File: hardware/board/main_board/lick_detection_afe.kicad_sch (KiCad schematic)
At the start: 77 parts, among them J3 Conn_Triaxial, U10 ADA4891-2, U13 ADS7049, U14 MAX4564EKA, U15 MAX4564EKA, U6 ADA4891-4, U7 LTC6268xS8-10, U8 REF2025, U9 TS5A9411DCKR

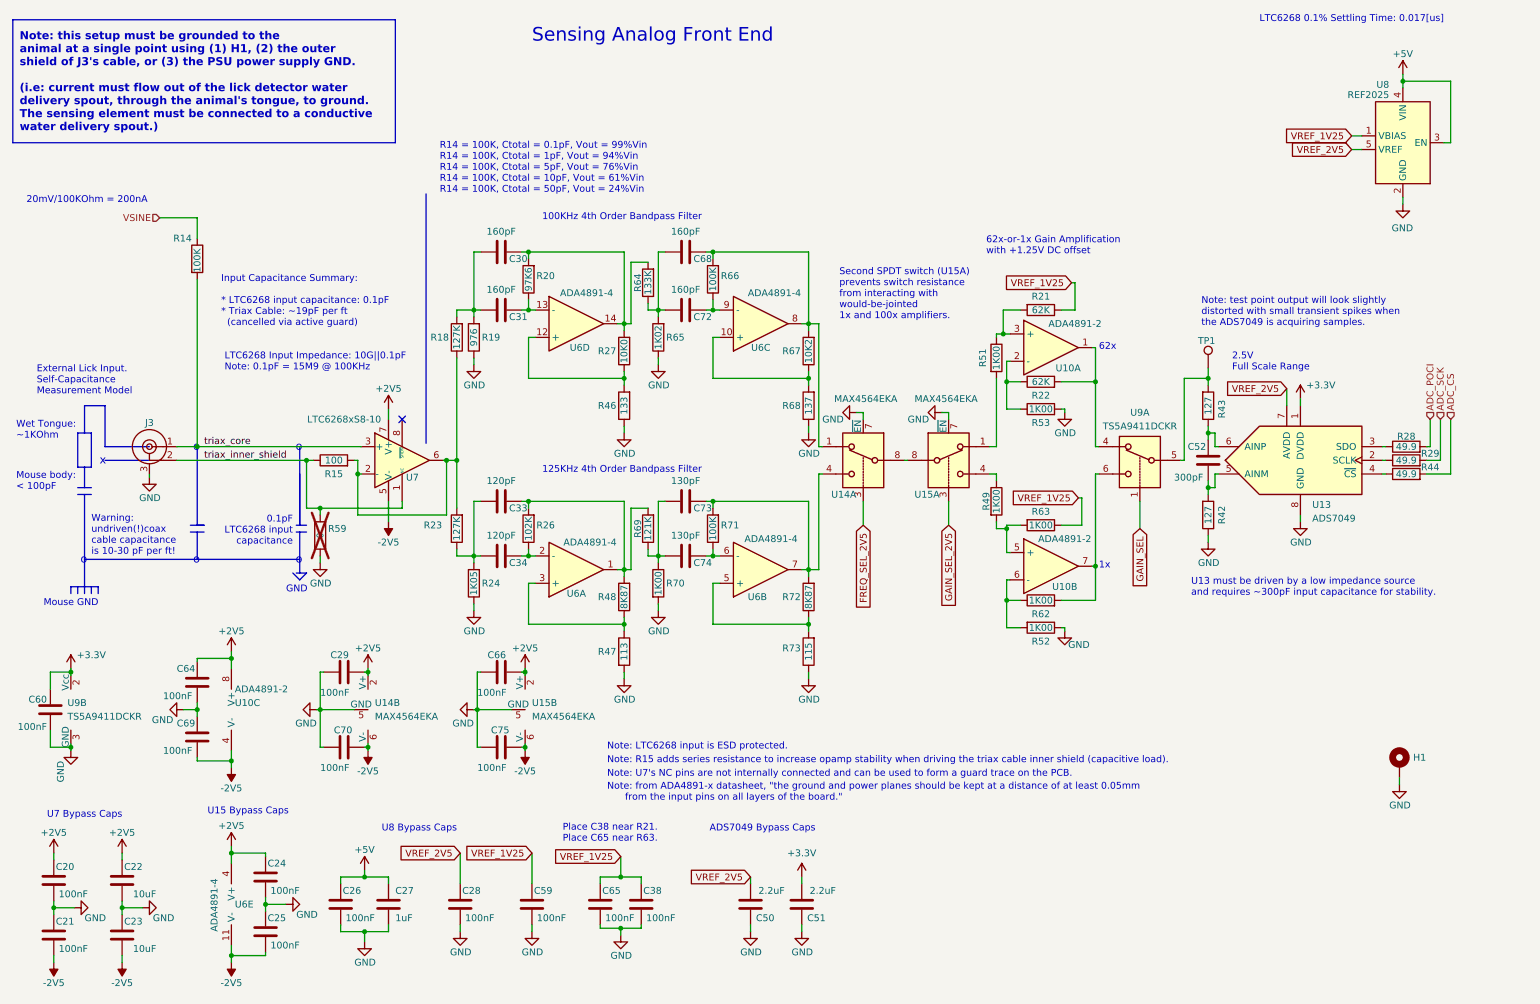
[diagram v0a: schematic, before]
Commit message: split board into two
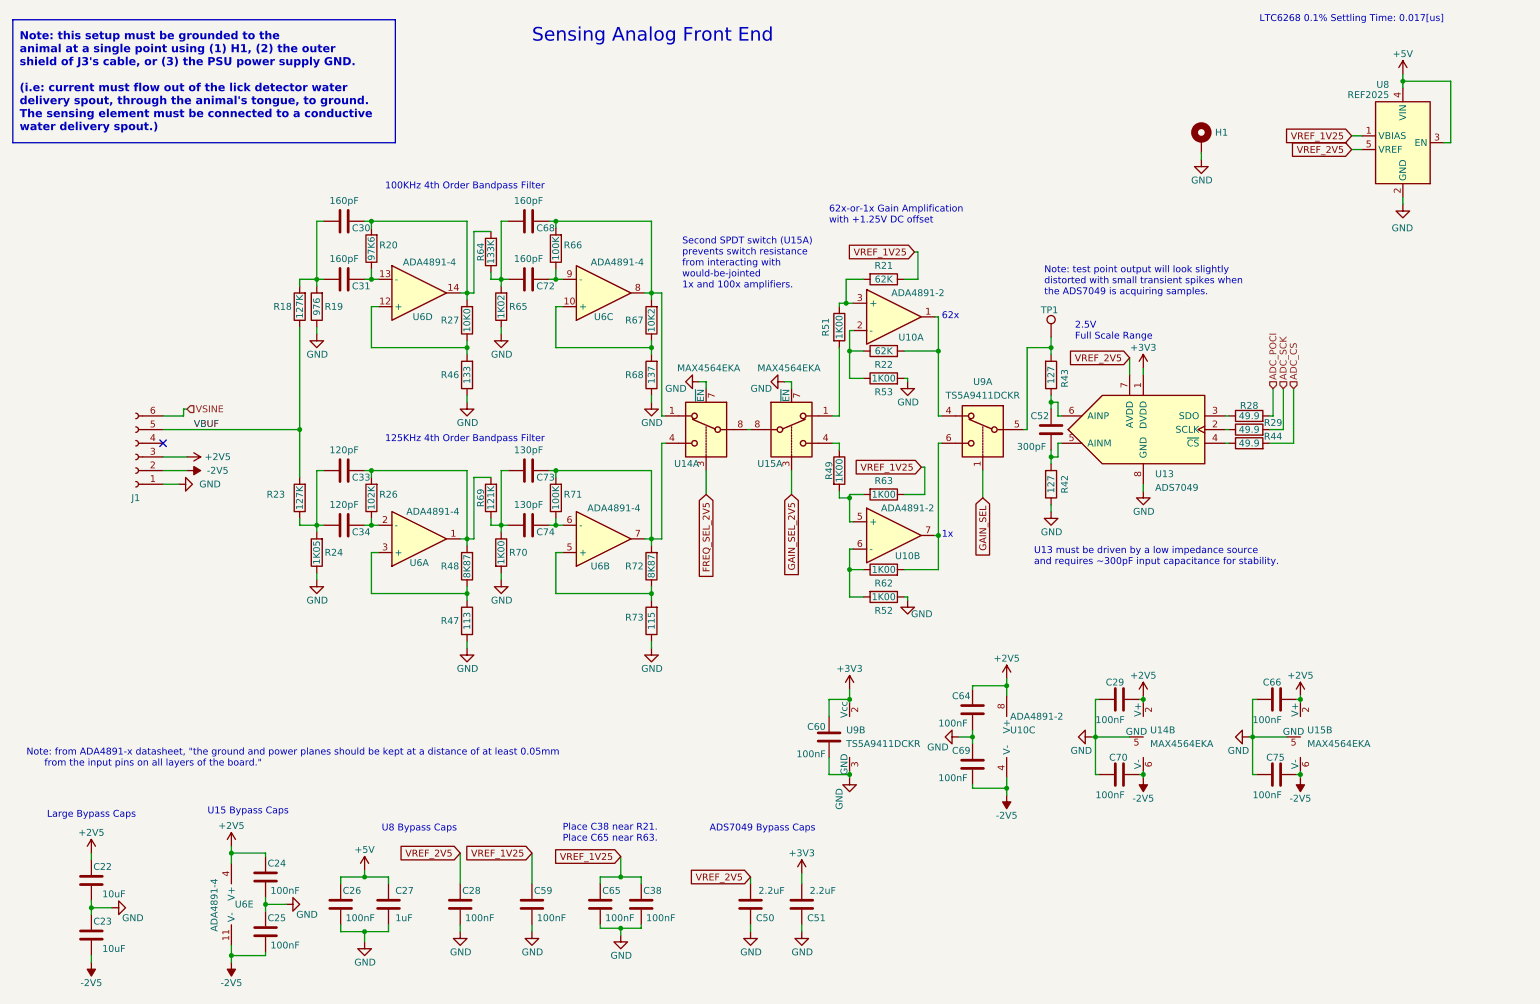
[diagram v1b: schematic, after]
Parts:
- removed C20, C21: 100nF, Capacitor_SMD:C_0402_1005Metric, symbol Device:C
- removed J3: Conn_Triaxial, kicad_component_library:TRB_Trompeter_CBBJR79A_Horizontal, symbol kicad_component_library:Conn_Triaxial
- removed R14: 100K, Resistor_SMD:R_1206_3216Metric, symbol Device:R
- removed R15: 100, Resistor_SMD:R_0402_1005Metric_Pad0.72x0.64mm_HandSolder, symbol Device:R
- removed R59: 0, Resistor_SMD:R_0402_1005Metric_Pad0.72x0.64mm_HandSolder, symbol Device:R
- removed U7: LTC6268xS8-10, Package_SO:SO-8_3.9x4.9mm_P1.27mm, symbol Amplifier_Operational:LTC6268xS8-10
- added J1: Conn_01x06_Female, Connector_JST:JST_SH_SM06B-SRSS-TB_1x06-1MP_P1.00mm_Horizontal, symbol Connector:Conn_01x06_Female
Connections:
- net +2V5: now also J1.3 (Pin_3)
- net -2V5: now also J1.2 (Pin_2)
- net GND: now also J1.1 (Pin_1)
- net VSINE: now also J1.6 (Pin_6)
- net VBUF: now reaches R18.1, R23.2
- net VBUF: now also J1.5 (Pin_5)
- net +3.3V renamed +3V3
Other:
- note added: "Large Bypass Caps"
- note removed: "0.1pF LTC6268 input capacitance"
- note removed: "20mV/100KOhm = 200nA"
- note removed: "External Lick Input. Self-Capacitance Measurement Model"
- note removed: "GND"
- note removed: "Input Capacitance Summary: * LTC6268 input capacitance: 0.1pF * Triax Cable: ~19pF per ft (cancelled via active guard)"
- note removed: "LTC6268 Input Impedance: 10G||0.1pF Note: 0.1pF = 15M9 @ 100KHz"
- note removed: "Mouse GND"
- note removed: "Mouse body: < 100pF"
- note removed: "Note: LTC6268 input is ESD protected."
- note removed: "Note: R15 adds series resistance to increase opamp stability when driving the triax cable inner shield (capacitive load)."
- note removed: "Note: U7's NC pins are not internally connected and can be used to form a guard trace on the PCB."
- note removed: "R14 = 100K, Ctotal = 0.1pF, Vout = 99%Vin R14 = 100K, Ctotal = 1pF, Vout = 94%Vin R14 = 100K, Ctotal = 5pF, Vout = 76%Vin R14 = 100K, Ctotal = 10pF, Vout = 61%Vin R14 = 100K, Ctotal = 50pF, Vout = 24%Vin"
- note removed: "U7 Bypass Caps"
- note removed: "Warning: undriven(!)coax cable capacitance is 10-30 pF per ft!"
- note removed: "Wet Tongue: ~1KOhm"
- note removed: "o"
- note removed: "x"
- moved on the sheet: C22, C23, C29, C30, C31, C33, C34, C52, C60, C64, C66, C68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

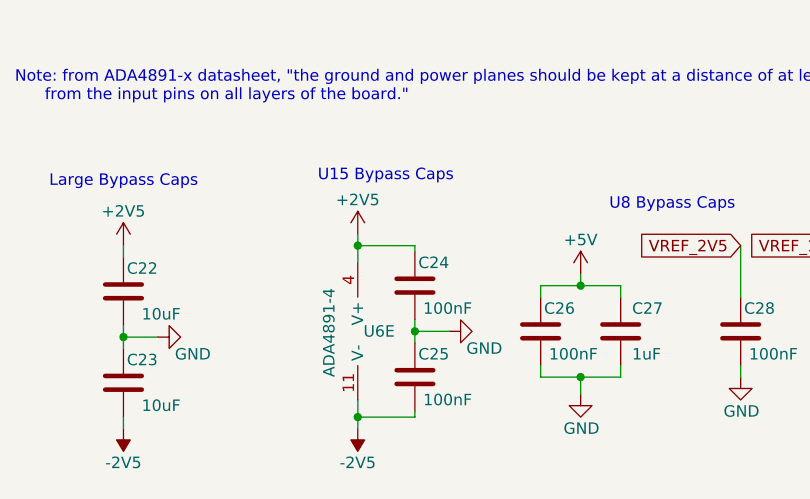
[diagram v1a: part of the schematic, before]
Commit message: update buffer board soldermask cutout
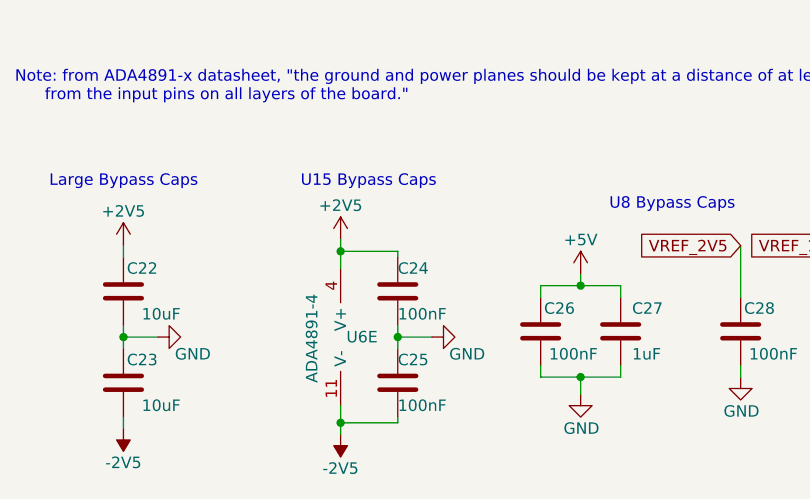
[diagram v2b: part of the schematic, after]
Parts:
- C22, C23: Alternate CL21B106KOQNNNE -> (none)
- C24, C25: footprint Capacitor_SMD:C_0603_1608Metric -> Capacitor_SMD:C_0402_1005Metric; Link https://www.digikey.com/en/products/detail/samsung-electro-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 -> https://www.digikey.com/en/products/detail/walsin-technolog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; Manufacturer Samsung Electro-Mechanics -> Walson Technology Corporation; Manufacturer Number CL10B104KB8NNNC -> 0402B104K160CT; Rated Voltage 50V -> 16V
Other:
- moved on the sheet: U6E

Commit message: add split pcba design
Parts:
- J1: Link https://www.newark.com/jst-japan-solderless-terminals/sm06b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 -> https://www.digikey.com/en/products/detail/jst-sales-americ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; Manufacturer (none) -> JST Sales America Inc.; Manufacturer Num SM06B-SRSS-TB(LF)(SN) -> (none); Manufacturer Number (none) -> SM06B-SRSS-TB; Vendor Newark -> (none); Vendor Num 33P8182 -> (none)
